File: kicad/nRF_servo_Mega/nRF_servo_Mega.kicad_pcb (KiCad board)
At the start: 2 copper layers, 85.1 x 53.3 mm, 12 parts, among them J1 Screw_Terminal_01x02, M1 Motor_Servo, M2 Motor_Servo, M3 Motor_Servo, M4 Motor_Servo, M5 Motor_Servo, M6 Motor_Servo, U1 NRF24L01_Breakout

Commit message: rf24PerformingRobotsTemplate_2023 transmits and receives reliably
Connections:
- XA1 pad GND4: unconnected-(XA1-SPI_GND-PadGND4) -> GND
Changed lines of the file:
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@@
   (net 86 "Net-(M6-PWM)")
   (net 87 "Net-(M4-PWM)")
-  (net 88 "unconnected-(XA1-SPI_GND-PadGND4)")
-  (net 89 "unconnected-(XA1-PadD8)")
+  (net 88 "unconnected-(XA1-PadD8)")
   (footprint "Connector_PinHeader_2.54mm:PinHeader_1x03_P2.54mm_Vertical" (layer "F.Cu")
     (at 39.37 30.48 90)
@@
     (fp_arc (start 94.488 -0.254) (mid 96.52 -0.914237) (end 98.552 -0.254)
       (stroke (width 0.15) (type solid)) (layer "F.CrtYd"))
-    (fp_arc (start 99.314 0.508) (mid 99.650928 1.077972) (end 99.8728 1.7018)
+    (fp_arc (start 99.314 0.508) (mid 99.650922 1.077974) (end 99.8728 1.7018)
       (stroke (width 0.15) (type solid)) (layer "F.CrtYd"))
     (fp_line (start -6.34 32.1936) (end -6.34 44.0036)
@@
       (net 63 "unconnected-(XA1-5V-Pad5V1)") (pinfunction "5V") (pintype "power_in+no_connect"))
     (pad "5V2" thru_hole oval (at 66.167 30.48 180) (size 3 1.7272) (drill 1.016 (offset 0.5 0)) (layers "*.Cu" "*.Mask")
-      (net 1 "unconnected-(XA1-SPI_5V-Pad5V2)") (pinfunction "SPI_5V") (pintype "power_in"))
+      (net 1 "unconnected-(XA1-SPI_5V-Pad5V2)") (pinfunction "SPI_5V") (pintype "power_in+no_connect"))
     (pad "5V3" thru_hole oval (at 93.98 50.8 180) (size 3 1.7272) (drill 1.016 (offset -0.5 0)) (layers "*.Cu" "*.Mask")
       (net 64 "unconnected-(XA1-5V-Pad5V3)") (pinfunction "5V") (pintype "power_in+no_connect"))
@@
       (net 78 "unconnected-(XA1-PadD7)") (pinfunction "D7") (pintype "bidirectional+no_connect"))
     (pad "D8" thru_hole oval (at 41.656 50.8 180) (size 1.7272 4) (drill 1.016) (layers "*.Cu" "*.Mask")
-      (net 89 "unconnected-(XA1-PadD8)") (pinfunction "D8") (pintype "bidirectional+no_connect"))
+      (net 88 "unconnected-(XA1-PadD8)") (pinfunction "D8") (pintype "bidirectional+no_connect"))
     (pad "D9" thru_hole oval (at 39.116 50.8 180) (size 1.7272 4) (drill 1.016) (layers "*.Cu" "*.Mask")
       (net 4 "unconnected-(XA1-PadD9)") (pinfunction "D9") (pintype "bidirectional+no_connect"))
@@
       (net 71 "GND") (pinfunction "GND") (pintype "power_in"))
     (pad "GND4" thru_hole rect (at 66.167 25.4 180) (size 3 1.7272) (drill 1.016 (offset 0.5 0)) (layers "*.Cu" "*.Mask")
-      (net 88 "unconnected-(XA1-SPI_GND-PadGND4)") (pinfunction "SPI_GND") (pintype "power_in"))
+      (net 71 "GND") (pinfunction "SPI_GND") (pintype "power_in"))
     (pad "GND5" thru_hole rect (at 93.98 7.62 180) (size 3 1.7272) (drill 1.016 (offset -0.5 0)) (layers "*.Cu" "*.Mask")
       (net 71 "GND") (pinfunction "GND") (pintype "power_in"))
@@
       (net 73 "unconnected-(XA1-RESET-PadRST1)") (pinfunction "RESET") (pintype "open_collector+no_connect"))
     (pad "RST2" thru_hole oval (at 63.627 25.4 180) (size 3 1.7272) (drill 1.016 (offset -0.5 0)) (layers "*.Cu" "*.Mask")
-      (net 51 "unconnected-(XA1-SPI_RESET-PadRST2)") (pinfunction "SPI_RESET") (pintype "open_collector"))
+      (net 51 "unconnected-(XA1-SPI_RESET-PadRST2)") (pinfunction "SPI_RESET") (pintype "open_collector+no_connect"))
     (pad "SCK" thru_hole oval (at 63.627 27.94 180) (size 3 1.7272) (drill 1.016 (offset -0.5 0)) (layers "*.Cu" "*.Mask")
       (net 79 "Net-(U1-SCK)") (pinfunction "SPI_SCK") (pintype "output"))

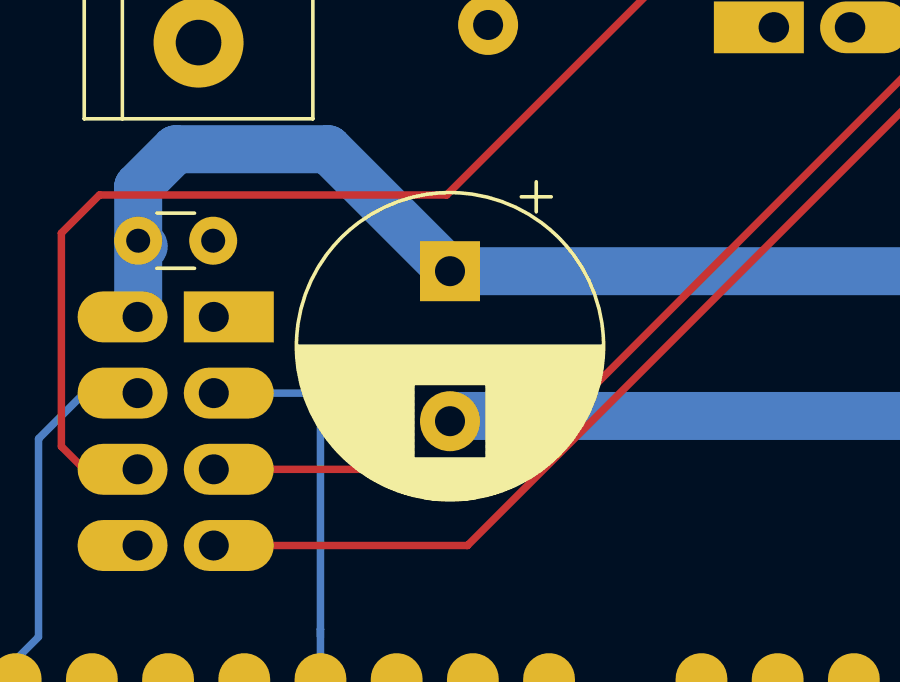
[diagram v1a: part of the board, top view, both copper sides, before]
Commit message: starting the Hobby RC and Motor Control shield
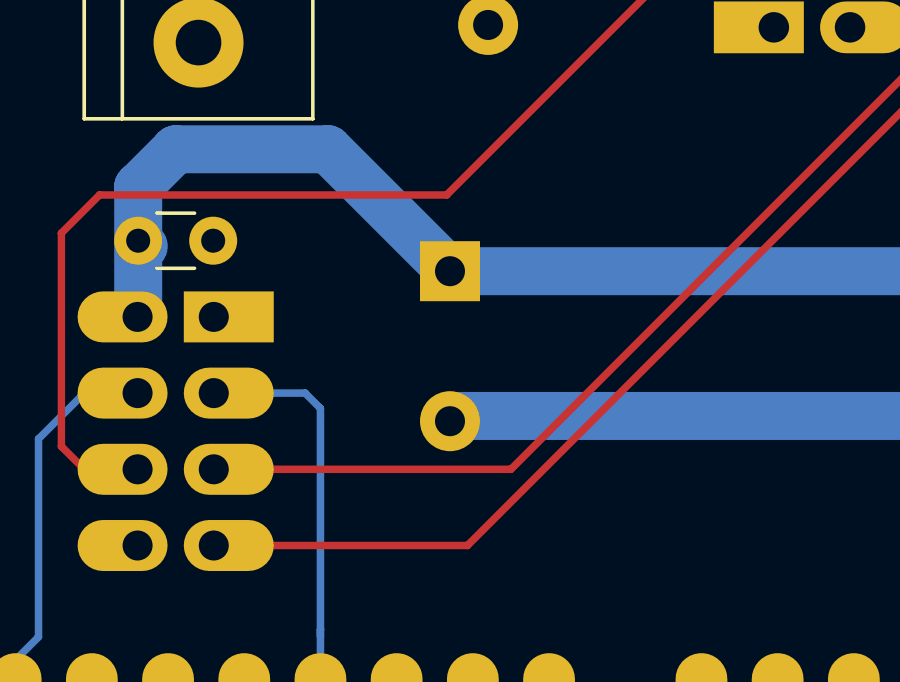
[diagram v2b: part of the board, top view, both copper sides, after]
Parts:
- C2: moved to B.Cu
- renumbered M4 to D16, M6 to D17, M5 to D18, M1 to D19, M2 to D21

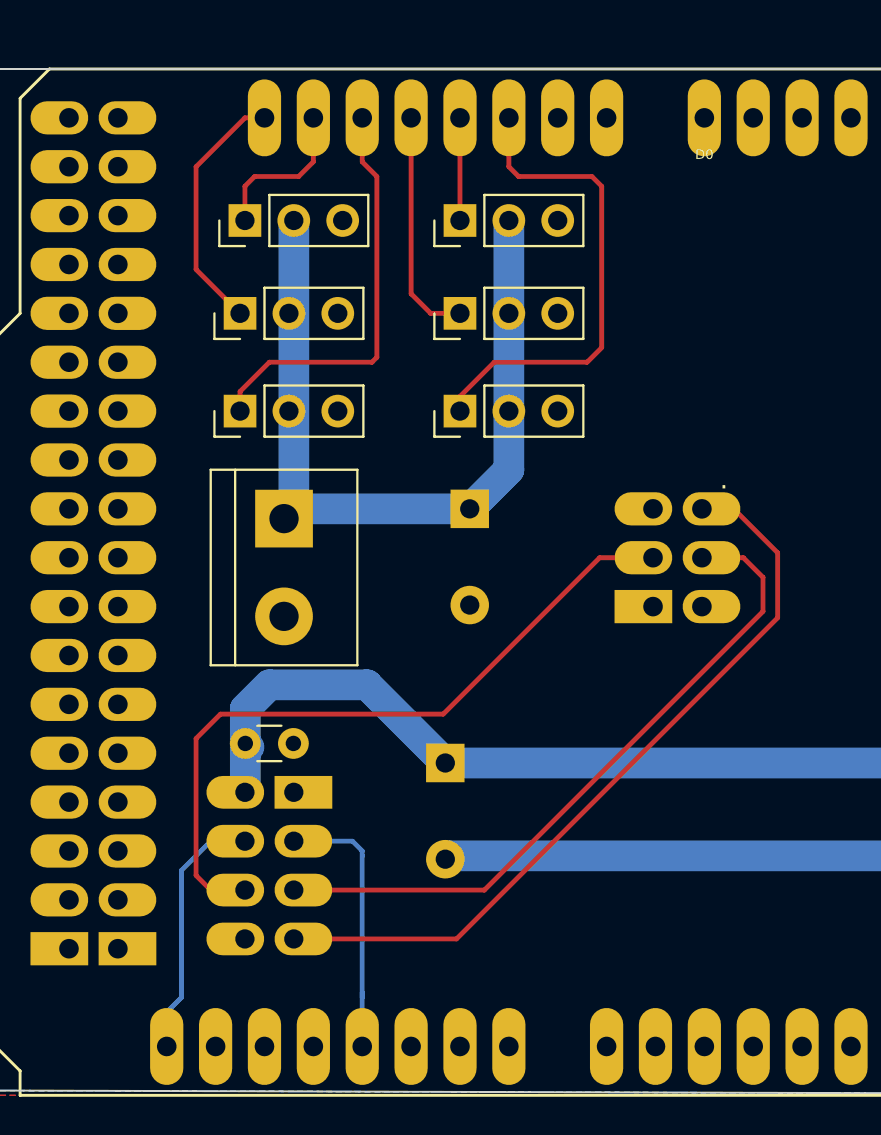
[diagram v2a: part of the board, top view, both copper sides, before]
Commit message: finished hobby rc and motor controller shield
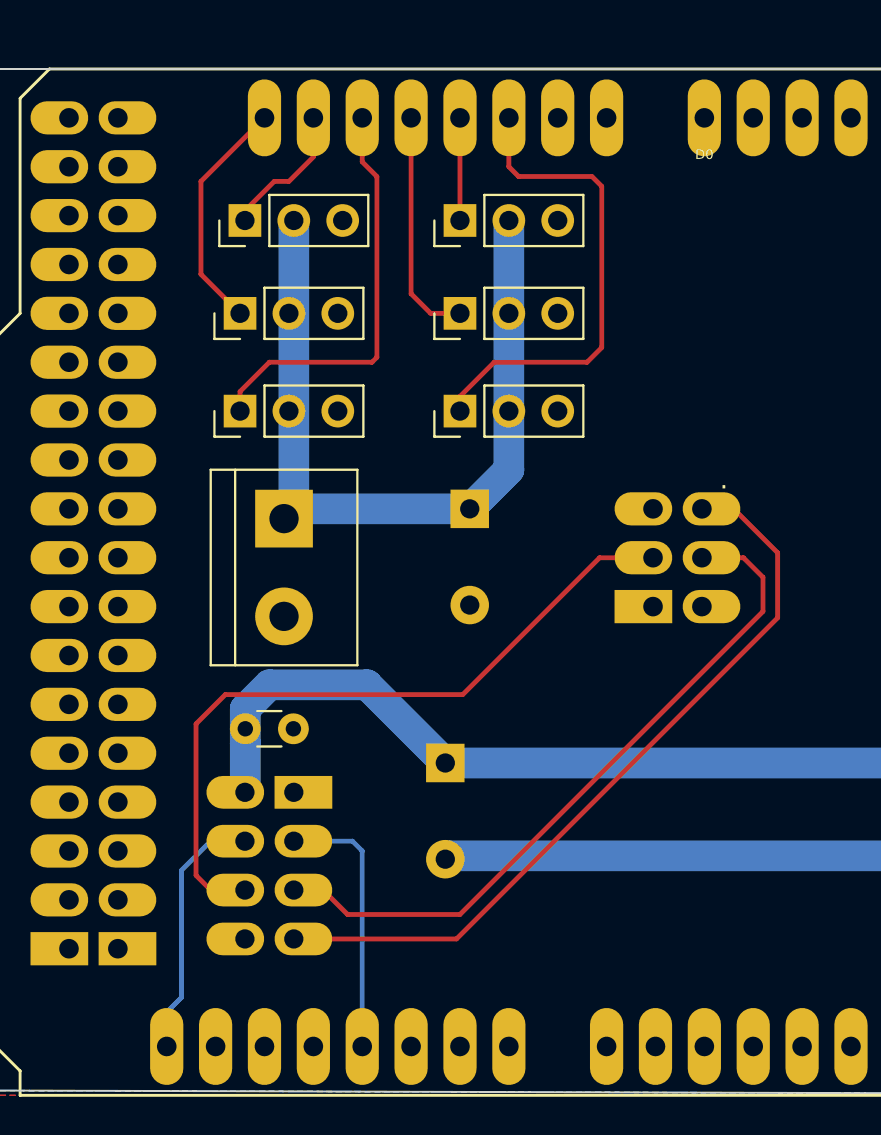
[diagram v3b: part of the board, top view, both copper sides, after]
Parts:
- moved C1 0.76 mm to (39.6, 52.1)
- renumbered D19 to M1, D21 to M2, D16 to M4, D18 to M5, D17 to M6
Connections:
- XA1 pad D20: Net-(M2-PWM) -> Net-(M3-PWM)
- XA1 pad D21: Net-(M3-PWM) -> Net-(M2-PWM)
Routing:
- net Net-(M3-PWM): track 8.15 -> 6.75 mm
- net Net-(U1-SCK): track 35.8 -> 36.8 mm
- net Net-(M2-PWM): track 13.2 -> 12.4 mm
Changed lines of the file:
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@@
     (pad_to_mask_clearance 0)
     (pcbplotparams
-      (layerselection 0x00010d0_ffffffff)
+      (layerselection 0x00010fc_ffffffff)
       (plot_on_all_layers_selection 0x0000000_00000000)
       (disableapertmacros false)
@@
     (property "ki_keywords" "Servo Motor")
     (attr through_hole)
-    (fp_text reference "D21" (at 0 -2.794 270) (layer "B.SilkS")
+    (fp_text reference "M2" (at 0 -2.794 270) (layer "B.SilkS")
         (effects (font (size 1.5 1.5) (thickness 0.15)) (justify mirror))
     )
@@
     (property "ki_keywords" "Servo Motor")
     (attr through_hole)
-    (fp_text reference "D19" (at 0 -2.794 90) (layer "B.SilkS")
+    (fp_text reference "M1" (at 0 -2.794 90) (layer "B.SilkS")
         (effects (font (size 1.5 1.5) (thickness 0.15)) (justify mirror))
     )
@@
     (property "ki_keywords" "Servo Motor")
     (attr through_hole)
-    (fp_text reference "D17" (at -0.508 10.16 180) (layer "B.SilkS")
+    (fp_text reference "M6" (at -0.508 10.16 180) (layer "B.SilkS")
         (effects (font (size 2 2) (thickness 0.15)) (justify mirror))
     )
@@
     (property "ki_keywords" "Servo Motor")
     (attr through_hole)
-    (fp_text reference "D18" (at -0.254 9.906 180) (layer "B.SilkS")
+    (fp_text reference "M5" (at -0.254 9.906 180) (layer "B.SilkS")
         (effects (font (size 2 2) (thickness 0.15)) (justify mirror))
     )
@@
     (property "ki_keywords" "Servo Motor")
     (attr through_hole)
-    (fp_text reference "D16" (at 0 9.906 180) (layer "B.SilkS")
+    (fp_text reference "M4" (at 0 9.906 180) (layer "B.SilkS")
         (effects (font (size 2 2) (thickness 0.15)) (justify mirror))
     )
@@
   )
   (footprint "Capacitor_THT:C_Disc_D3.0mm_W1.6mm_P2.50mm" (layer "F.Cu")
-    (at 39.644 52.832)
+    (at 39.644 52.07)
     (descr "C, Disc series, Radial, pin pitch=2.50mm, , diameter*width=3.0*1.6mm^2, Capacitor, http://www.vishay.com/docs/45233/krseries.pdf")
     (tags "C Disc series Radial pin pitch 2.50mm  diameter 3.0mm width 1.6mm Capacitor")
@@
       (net 84 "Net-(M1-PWM)") (pinfunction "D19/RX1") (pintype "bidirectional"))
     (pad "D20" thru_hole oval (at 83.82 50.8 180) (size 1.7272 4) (drill 1.016) (layers "*.Cu" "*.Mask")
-      (net 83 "Net-(M2-PWM)") (pinfunction "D20/SDA") (pintype "bidirectional"))
+      (net 82 "Net-(M3-PWM)") (pinfunction "D20/SDA") (pintype "bidirectional"))
     (pad "D21" thru_hole oval (at 86.36 50.8 180) (size 1.7272 4) (drill 1.016) (layers "*.Cu" "*.Mask")
-      (net 82 "Net-(M3-PWM)") (pinfunction "D21/SCL") (pintype "bidirectional"))
+      (net 83 "Net-(M2-PWM)") (pinfunction "D21/SCL") (pintype "bidirectional"))
     (pad "D22" thru_hole oval (at 93.98 48.26 180) (size 3 1.7272) (drill 1.016 (offset -0.5 0)) (layers "*.Cu" "*.Mask")
       (net 18 "unconnected-(XA1-PadD22)") (pinfunction "D22") (pintype "bidirectional+no_connect"))
@@
         (effects (font (size 1 1) (thickness 0.15)) (justify mirror))
     )
-    (fp_text value "470 uF" (at 1.524 -8.128) (layer "F.Fab")
+    (fp_text value "470 uF" (at 1.524 -8.128) (layer "B.SilkS")
         (effects (font (size 1 1) (thickness 0.15)) (justify mirror))
     )
@@
   (segment (start 42.164 62.992) (end 50.621167 62.992) (width 0.25) (layer "F.Cu") (net 46))
   (segment (start 65.024 40.64) (end 63.373 40.64) (width 0.25) (layer "F.Cu") (net 46))
-  (segment (start 37.846 60.452) (end 37.084 59.69) (width 0.25) (layer "F.Cu") (net 47))
-  (segment (start 38.354 51.308) (end 49.928 51.308) (width 0.25) (layer "F.Cu") (net 47))
-  (segment (start 37.084 52.578) (end 38.354 51.308) (width 0.25) (layer "F.Cu") (net 47))
-  (segment (start 49.928 51.308) (end 58.056 43.18) (width 0.25) (layer "F.Cu") (net 47))
-  (segment (start 58.056 43.18) (end 60.833 43.18) (width 0.25) (layer "F.Cu") (net 47))
-  (segment (start 39.624 60.452) (end 37.846 60.452) (width 0.25) (layer "F.Cu") (net 47))
-  (segment (start 37.084 59.69) (end 37.084 52.578) (width 0.25) (layer "F.Cu") (net 47))
-  (segment (start 33.2075 58.6075) (end 33.02 58.42) (width 0.25) (layer "F.Cu") (net 50))
+  (segment (start 37.084 51.816) (end 37.084 59.69) (width 0.25) (layer "F.Cu") (net 47))
+  (segment (start 60.833 43.18) (end 58.056 43.18) (width 0.25) (layer "F.Cu") (net 47))
+  (segment (start 50.944 50.292) (end 38.608 50.292) (width 0.25) (layer "F.Cu") (net 47))
+  (segment (start 37.084 59.69) (end 37.846 60.452) (width 0.25) (layer "F.Cu") (net 47))
+  (segment (start 37.846 60.452) (end 39.624 60.452) (width 0.25) (layer "F.Cu") (net 47))
+  (segment (start 58.056 43.18) (end 50.944 50.292) (width 0.25) (layer "F.Cu") (net 47))
+  (segment (start 38.608 50.292) (end 37.084 51.816) (width 0.25) (layer "F.Cu") (net 47))
   (segment (start 51.308 40.64) (end 42.164 40.64) (width 1.6) (layer "B.Cu") (net 56))
   (segment (start 42.164 40.64) (end 41.656 41.148) (width 1.6) (layer "B.Cu") (net 56))
@@
   (segment (start 40.894 49.784) (end 39.644 51.034) (width 1.6) (layer "B.Cu") (net 57))
   (segment (start 83.312 53.848) (end 91.44 61.976) (width 1.6) (layer "B.Cu") (net 57))
-  (segment (start 39.8315 53.0195) (end 39.644 52.832) (width 1.6) (layer "B.Cu") (net 57))
   (segment (start 91.44 61.976) (end 91.44 68.58) (width 1.6) (layer "B.Cu") (net 57))
   (segment (start 39.644 55.352) (end 39.624 55.372) (width 1.6) (layer "B.Cu") (net 57))
@@
   (segment (start 50.038 58.848) (end 50.212 58.674) (width 1.6) (layer "B.Cu") (net 71))
   (segment (start 50.212 58.674) (end 81.44 58.674) (width 1.6) (layer "B.Cu") (net 71))
-  (segment (start 66.548 45.974) (end 66.548 44.196) (width 0.25) (layer "F.Cu") (net 79))
-  (segment (start 42.164 60.452) (end 52.07 60.452) (width 0.25) (layer "F.Cu") (net 79))
-  (segment (start 65.532 43.18) (end 63.373 43.18) (width 0.25) (layer "F.Cu") (net 79))
-  (segment (start 52.07 60.452) (end 66.548 45.974) (width 0.25) (layer "F.Cu") (net 79))
-  (segment (start 66.548 44.196) (end 65.532 43.18) (width 0.25) (layer "F.Cu") (net 79))
+  (segment (start 44.958 61.722) (end 43.688 60.452) (width 0.25) (layer "F.Cu") (net 79))
+  (segment (start 43.688 60.452) (end 42.164 60.452) (width 0.25) (layer "F.Cu") (net 79))
+  (segment (start 65.532 43.18) (end 66.548 44.196) (width 0.25) (layer "F.Cu") (net 79))
+  (segment (start 50.8 61.722) (end 44.958 61.722) (width 0.25) (layer "F.Cu") (net 79))
+  (segment (start 66.548 44.196) (end 66.548 45.974) (width 0.25) (layer "F.Cu") (net 79))
+  (segment (start 66.548 45.974) (end 50.8 61.722) (width 0.25) (layer "F.Cu") (net 79))
+  (segment (start 63.373 43.18) (end 65.532 43.18) (width 0.25) (layer "F.Cu") (net 79))
   (segment (start 45.212 57.912) (end 45.72 58.42) (width 0.25) (layer "B.Cu") (net 80))
-  (segment (start 45.72 58.674) (end 45.72 65.786) (width 0.25) (layer "B.Cu") (net 80))
-  (segment (start 45.72 65.786) (end 45.72 66.04) (width 0.25) (layer "B.Cu") (net 80))
-  (segment (start 45.72 65.786) (end 45.72 68.58) (width 0.25) (layer "B.Cu") (net 80))
-  (segment (start 45.72 58.42) (end 45.72 58.674) (width 0.25) (layer "B.Cu") (net 80))
+  (segment (start 45.72 58.42) (end 45.72 68.58) (width 0.25) (layer "B.Cu") (net 80))
   (segment (start 42.164 57.912) (end 45.212 57.912) (width 0.25) (layer "B.Cu") (net 80))
   (segment (start 36.322 59.436) (end 36.322 66.04) (width 0.25) (layer "B.Cu") (net 81))
@@
   (segment (start 37.846 57.912) (end 36.322 59.436) (width 0.25) (layer "B.Cu") (net 81))
   (segment (start 35.56 68.58) (end 35.56 66.802) (width 0.25) (layer "B.Cu") (net 81))
-  (segment (start 43.18 20.32) (end 43.18 22.606) (width 0.25) (layer "F.Cu") (net 82))
-  (segment (start 42.418 23.368) (end 40.132 23.368) (width 0.25) (layer "F.Cu") (net 82))
-  (segment (start 39.624 23.876) (end 39.624 25.654) (width 0.25) (layer "F.Cu") (net 82))
-  (segment (start 43.18 22.606) (end 42.418 23.368) (width 0.25) (layer "F.Cu") (net 82))
-  (segment (start 40.132 23.368) (end 39.624 23.876) (width 0.25) (layer "F.Cu") (net 82))
-  (segment (start 37.084 28.194) (end 39.37 30.48) (width 0.25) (layer "F.Cu") (net 83))
-  (segment (start 37.084 22.86) (end 37.084 28.194) (width 0.25) (layer "F.Cu") (net 83))
-  (segment (start 39.624 20.32) (end 37.084 22.86) (width 0.25) (layer "F.Cu") (net 83))
-  (segment (start 40.64 20.32) (end 39.624 20.32) (width 0.25) (layer "F.Cu") (net 83))
+  (segment (start 41.148 23.622) (end 39.624 25.146) (width 0.25) (layer "F.Cu") (net 82))
+  (segment (start 43.18 20.32) (end 43.18 22.352) (width 0.25) (layer "F.Cu") (net 82))
+  (segment (start 43.18 22.352) (end 41.91 23.622) (width 0.25) (layer "F.Cu") (net 82))
+  (segment (start 41.91 23.622) (end 41.148 23.622) (width 0.25) (layer "F.Cu") (net 82))
+  (segment (start 37.338 28.448) (end 37.338 23.622) (width 0.25) (layer "F.Cu") (net 83))
+  (segment (start 37.338 23.622) (end 40.64 20.32) (width 0.25) (layer "F.Cu") (net 83))
+  (segment (start 39.37 30.48) (end 37.338 28.448) (width 0.25) (layer "F.Cu") (net 83))
   (segment (start 39.37 34.544) (end 40.894 33.02) (width 0.25) (layer "F.Cu") (net 84))
   (segment (start 39.37 35.56) (end 39.37 34.544) (width 0.25) (layer "F.Cu") (net 84))

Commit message: added New Media Art
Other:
- board text added: "+"
- board text added: "-"
- board text added: "P"

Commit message: rev 2 of arduino shield hobby rc and motor control
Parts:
- renumbered M4 to D16, M6 to D17, M5 to D18
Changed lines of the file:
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@@
 		(descr "Through hole straight pin header, 1x03, 2.54mm pitch, single row")
 		(tags "Through hole pin header THT 1x03 2.54mm single row")
-		(property "Reference" "M6"
-			(at -0.508 10.16 180)
+		(property "Reference" "D17"
+			(at 0.154 10.7 180)
 			(layer "B.SilkS")
 			(effects
@@
 		(descr "Through hole straight pin header, 1x03, 2.54mm pitch, single row")
 		(tags "Through hole pin header THT 1x03 2.54mm single row")
-		(property "Reference" "M5"
-			(at -0.254 9.906 180)
+		(property "Reference" "D18"
+			(at -0.02 10.7 180)
 			(layer "B.SilkS")
 			(effects
@@
 		(descr "Through hole straight pin header, 1x03, 2.54mm pitch, single row")
 		(tags "Through hole pin header THT 1x03 2.54mm single row")
-		(property "Reference" "M4"
-			(at 0 9.906 180)
+		(property "Reference" "D16"
+			(at 0.06 10.7 180)
 			(layer "B.SilkS")
 			(effects
@@
 		(fp_arc
 			(start 99.314 0.508)
-			(mid 99.650926 1.077973)
+			(mid 99.650928 1.077972)
 			(end 99.8728 1.7018)
 			(stroke
@@
 		(tags "CP Radial series Radial pin pitch 5.00mm  diameter 10mm Electrolytic Capacitor")
 		(property "Reference" "C3"
-			(at -0.254 -5.842 0)
+			(at 9.86 -3.192 0)
 			(layer "B.SilkS")
 			(effects
@@
 		)
 		(property "Value" "470 uF"
-			(at -2.032 -6.604 180)
+			(at 8.36 -4.692 180)
 			(layer "B.SilkS")
 			(effects
@@
 		)
 	)
-	(gr_text_box "nRF Servo Mega\nMichael Shiloh 2024, 2025\nGPLv3 Applies\n\nRevision 0.1 March 2025\n"
+	(gr_text_box "nRF Servo Mega\nMichael Shiloh 2024, 2025\nGPLv3 Applies\n\nRevision 0.2 Sept 2025\n"
 		(start 72.192 34.29)
 		(end 106.426 48.808)

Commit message: example of bad solder joint
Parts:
- renumbered M1 to D19, M2 to D21
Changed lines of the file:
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@@
 		(descr "Through hole straight pin header, 1x03, 2.54mm pitch, single row")
 		(tags "Through hole pin header THT 1x03 2.54mm single row")
-		(property "Reference" "M2"
-			(at 0 -2.794 -90)
+		(property "Reference" "D21"
+			(at 0 -2.794 270)
 			(layer "B.SilkS")
 			(effects
@@
 		(descr "Through hole straight pin header, 1x03, 2.54mm pitch, single row")
 		(tags "Through hole pin header THT 1x03 2.54mm single row")
-		(property "Reference" "M1"
+		(property "Reference" "D19"
 			(at 0 -2.794 90)
 			(layer "B.SilkS")
